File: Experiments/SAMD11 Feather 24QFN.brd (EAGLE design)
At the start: 50.8 x 22.9 mm, 37 parts, among them IC1 ATSAMD11D14A-MUT, J1 10118193-0001LF, Q1 DMG341, SW1 SPST_TACT-KMR2, U1 AP2112-3.3, U2 MCP73831T-2ACI/OT, X1 JSTPH, X2 2x5 0.05" SWD

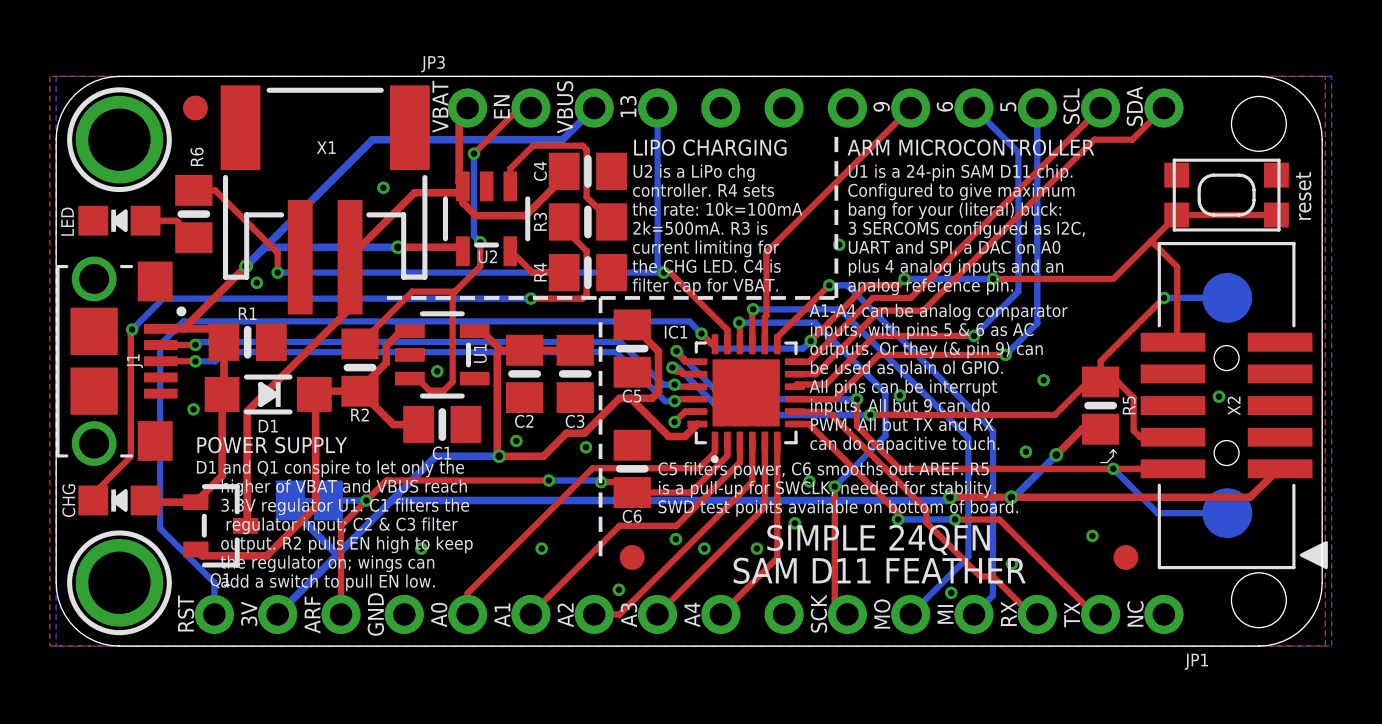
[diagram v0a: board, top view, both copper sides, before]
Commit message: fix swdio/swclk mixup
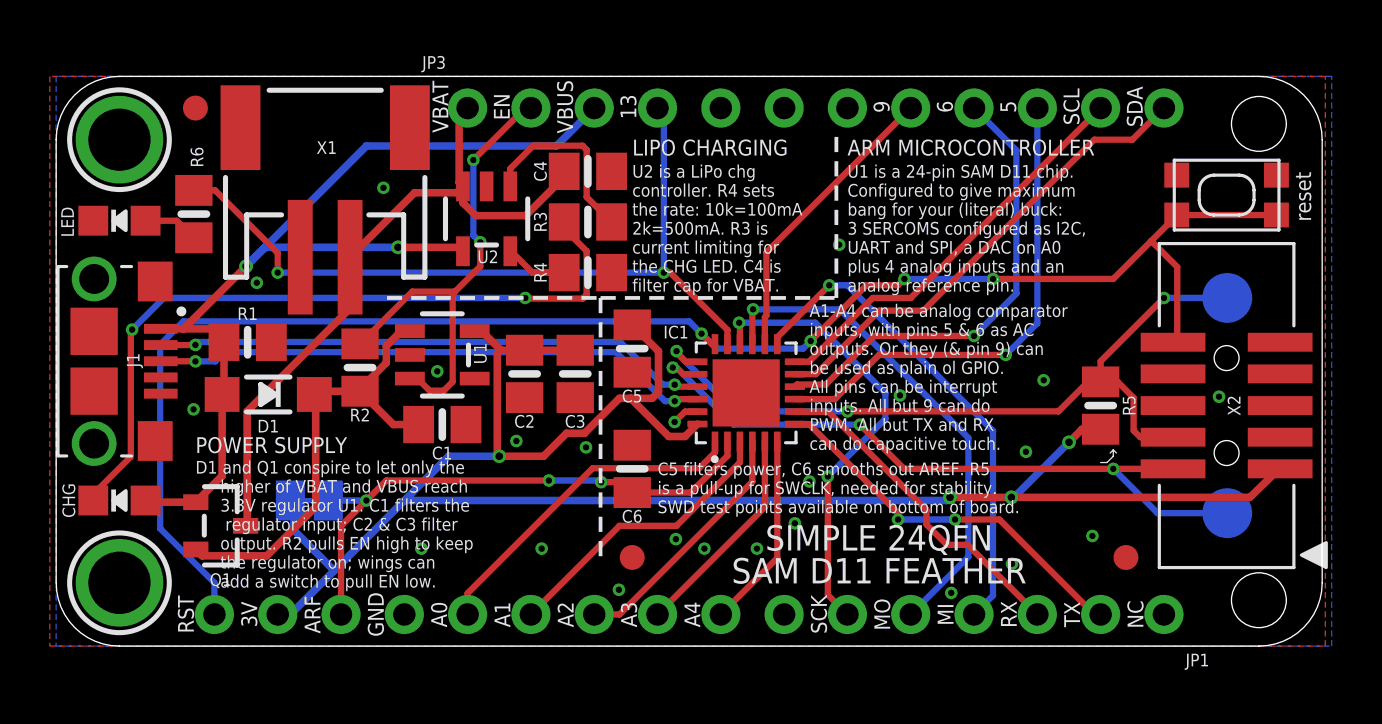
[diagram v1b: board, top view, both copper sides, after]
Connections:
- net SWCLK: now also IC1.19; no longer IC1.20
- net SWDIO: now also IC1.20; no longer IC1.19
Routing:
- net SWDIO: track 28.9 -> 28.2 mm
